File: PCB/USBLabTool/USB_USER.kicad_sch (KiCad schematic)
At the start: 15 parts, among them J19 USB_C_Receptacle, U17 TCPP01-M12

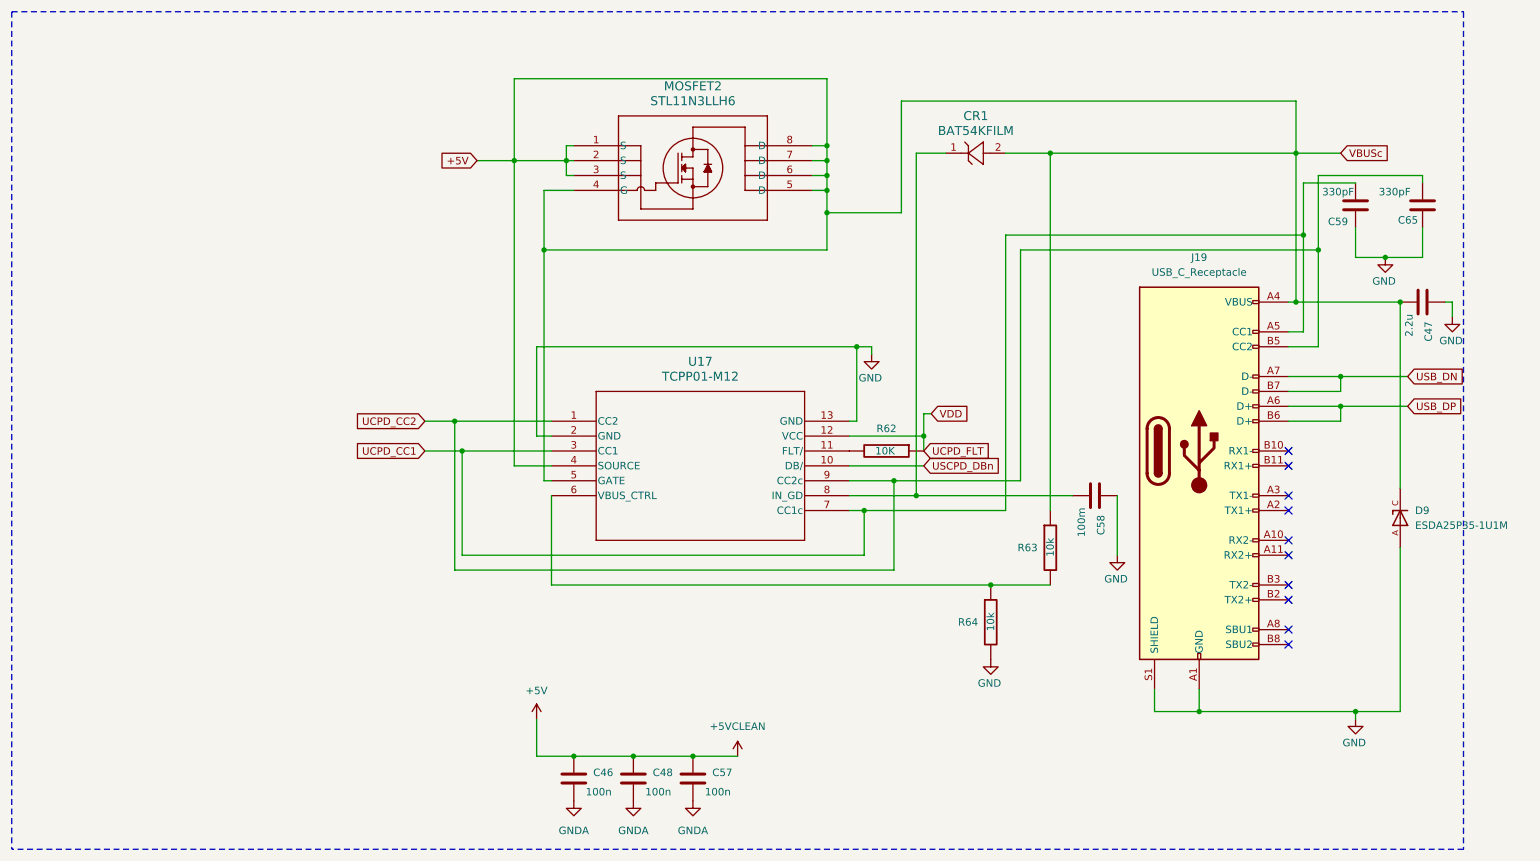
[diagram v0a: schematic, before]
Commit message: update MCU and USB, fix some footprints
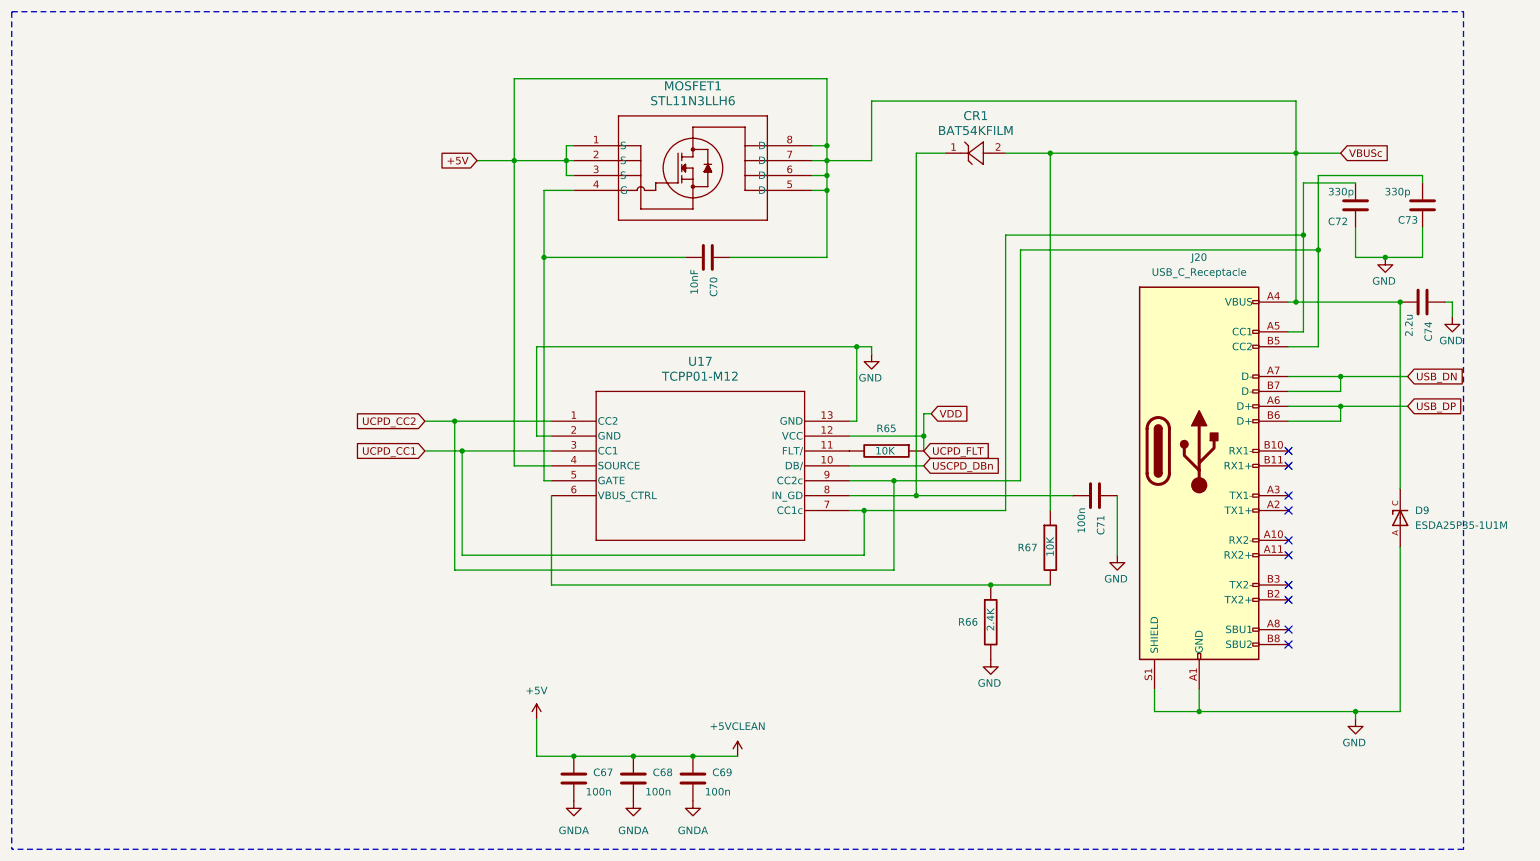
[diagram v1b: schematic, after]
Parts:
- added C70: 10nF, Capacitor_SMD:C_0603_1608Metric_Pad1.08x0.95mm_HandSolder, symbol Device:C
- C71: renamed from C58; value 100m -> 100n
- C72: renamed from C59; value 330pF -> 330p; footprint Capacitor_SMD:C_0603_1608Metric_Pad1.08x0.95mm_HandSolder -> Capacitor_SMD:C_0201_0603Metric_Pad0.64x0.40mm_HandSolder
- C73: renamed from C65; value 330pF -> 330p; footprint Capacitor_SMD:C_0603_1608Metric_Pad1.08x0.95mm_HandSolder -> Capacitor_SMD:C_0201_0603Metric_Pad0.64x0.40mm_HandSolder
- CR1: footprint SOD-523_STM -> Diode_SMD:D_SOD-523
- D9: footprint ESDA25P35-1U1M:TVS_ESDA25P35-1U1M -> footprintsgit:TVS_ESDA25P35-1U1M
- J20: renamed from J19; footprint footprints:CONN RCP USB3.1 TYPEC 24P SMD RA-632723300011 -> footprintsgit:CONN RCP USB3.1 TYPEC 24P SMD RA-632723300011
- R65: renamed from R62; footprint (none) -> Resistor_SMD:R_0603_1608Metric
- R66: renamed from R64; value 10k -> 2.4K; footprint (none) -> Resistor_SMD:R_0603_1608Metric
- R67: renamed from R63; value 10k -> 10K; footprint (none) -> Resistor_SMD:R_0603_1608Metric
- renumbered C46 to C67, C48 to C68, C57 to C69, C47 to C74, MOSFET2 to MOSFET1
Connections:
- net +5V: now also C70.1; no longer MOSFET1.4 (G), U17.5 (GATE)
- new net: C70.2, MOSFET1.4 (G), U17.5 (GATE)

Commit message: add usb protection
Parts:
- added D10: USBLC6-2SC6, PCM_Package_TO_SOT_SMD_AKL:SOT-23-6, symbol PCM_Diode_TVS_AKL:USBLC6-2SC6
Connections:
- net GND: now also D10.2 (VN)
- net USB_DN renamed D-
- net D-: now also D10.1 (L1), D10.6 (L1)
- net USB_DP renamed D+
- net D+: now also D10.3 (L2), D10.4 (L2)
- no-connect marks 10 -> 11
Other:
- moved on the sheet: R66

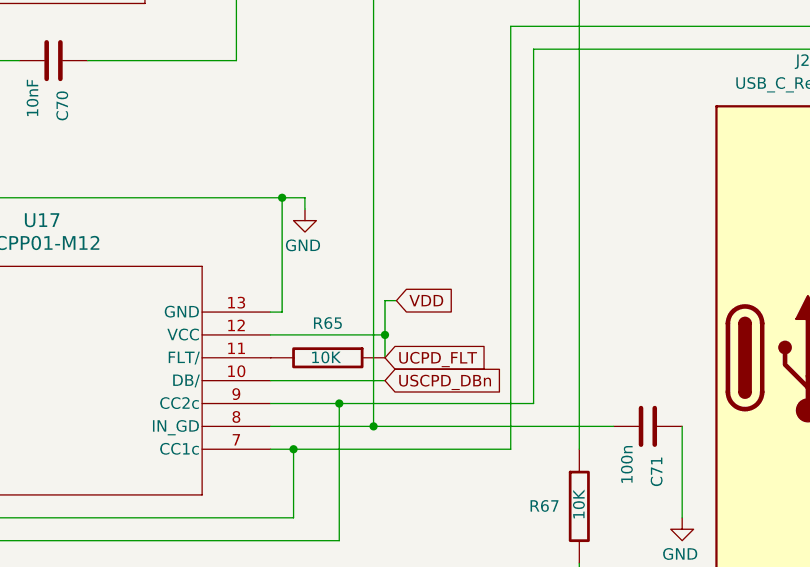
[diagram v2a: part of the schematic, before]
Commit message: add NRST button and change MCU pins as latest
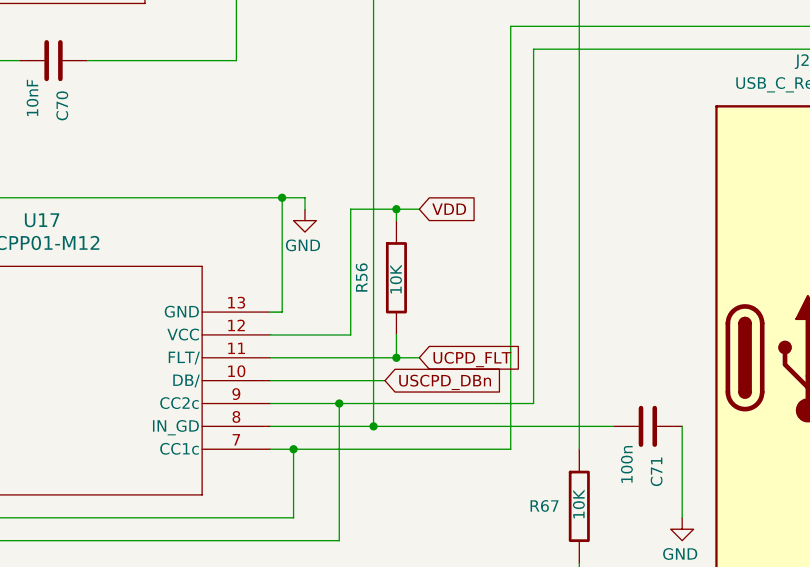
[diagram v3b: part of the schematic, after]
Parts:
- removed R65: 10K, Resistor_SMD:R_0603_1608Metric, symbol freetronics_schematic:R
- added R56: 10K, Resistor_SMD:R_0603_1608Metric, symbol freetronics_schematic:R
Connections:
- net UCPD_FLT: now also U17.11 (FLT/), R56.2; no longer U17.12 (VCC)
- new net VDD: R56.1, U17.12 (VCC)
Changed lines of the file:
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@@
 	)
 	(junction
+		(at 189.23 78.74)
+		(diameter 0)
+		(color 0 0 0 0)
+	)
+	(junction
 		(at 171.45 50.8)
 		(diameter 0)
@@
 	)
 	(junction
-		(at 251.46 44.45)
+		(at 189.23 95.25)
 		(diameter 0)
 		(color 0 0 0 0)
 	)
 	(junction
-		(at 171.45 48.26)
+		(at 251.46 44.45)
 		(diameter 0)
 		(color 0 0 0 0)
 	)
 	(junction
-		(at 176.53 77.47)
+		(at 171.45 48.26)
 		(diameter 0)
 		(color 0 0 0 0)
 	)
 	(junction
-		(at 187.96 92.71)
+		(at 176.53 77.47)
 		(diameter 0)
 		(color 0 0 0 0)
@@
 	(wire
 		(pts
-			(xy 187.96 88.9) (xy 187.96 92.71)
-		)
-		(stroke
-			(width 0)
-			(type default)
-		)
-	)
-	(wire
-		(pts
 			(xy 111.76 102.87) (xy 124.46 102.87)
 		)
@@
 	(wire
 		(pts
-			(xy 251.46 69.85) (xy 251.46 44.45)
+			(xy 184.15 78.74) (xy 184.15 92.71)
 		)
 		(stroke
@@
 	(wire
 		(pts
-			(xy 259.08 85.09) (xy 259.08 82.55)
+			(xy 251.46 69.85) (xy 251.46 44.45)
 		)
 		(stroke
@@
 	(wire
 		(pts
-			(xy 168.91 48.26) (xy 171.45 48.26)
+			(xy 259.08 85.09) (xy 259.08 82.55)
 		)
 		(stroke
@@
 	(wire
 		(pts
-			(xy 171.45 45.72) (xy 179.07 45.72)
+			(xy 168.91 48.26) (xy 171.45 48.26)
 		)
 		(stroke
@@
 	(wire
 		(pts
-			(xy 107.95 90.17) (xy 124.46 90.17)
+			(xy 171.45 45.72) (xy 179.07 45.72)
 		)
 		(stroke
@@
 	(wire
 		(pts
-			(xy 187.96 88.9) (xy 189.23 88.9)
+			(xy 107.95 90.17) (xy 124.46 90.17)
 		)
 		(stroke
@@
 	(wire
 		(pts
+			(xy 189.23 95.25) (xy 191.77 95.25)
+		)
+		(stroke
+			(width 0)
+			(type default)
+		)
+	)
+	(wire
+		(pts
 			(xy 255.27 60.96) (xy 255.27 48.26)
 		)
@@
 	(wire
 		(pts
+			(xy 184.15 78.74) (xy 189.23 78.74)
+		)
+		(stroke
+			(width 0)
+			(type default)
+		)
+	)
+	(wire
+		(pts
 			(xy 123.19 62.23) (xy 123.19 100.33)
 		)
@@
 	(wire
 		(pts
-			(xy 102.87 95.25) (xy 109.22 95.25)
+			(xy 189.23 78.74) (xy 189.23 80.01)
 		)
 		(stroke
@@
 	(wire
 		(pts
-			(xy 111.76 102.87) (xy 111.76 119.38)
+			(xy 102.87 95.25) (xy 109.22 95.25)
 		)
 		(stroke
@@
 	(wire
 		(pts
-			(xy 207.01 144.78) (xy 207.01 129.54)
+			(xy 111.76 102.87) (xy 111.76 119.38)
 		)
 		(stroke
@@
 	(wire
 		(pts
-			(xy 123.19 50.8) (xy 128.27 50.8)
+			(xy 207.01 144.78) (xy 207.01 129.54)
 		)
 		(stroke
@@
 	(wire
 		(pts
-			(xy 234.95 135.89) (xy 234.95 139.7)
+			(xy 123.19 50.8) (xy 128.27 50.8)
 		)
 		(stroke
@@
 	(wire
 		(pts
-			(xy 187.96 92.71) (xy 187.96 95.25)
+			(xy 234.95 135.89) (xy 234.95 139.7)
 		)
 		(stroke
@@
 	(wire
 		(pts
+			(xy 189.23 95.25) (xy 189.23 92.71)
+		)
+		(stroke
+			(width 0)
+			(type default)
+		)
+	)
+	(wire
+		(pts
 			(xy 182.88 129.54) (xy 185.42 129.54)
 		)
@@
 		)
 	)
+	(wire
+		(pts
+			(xy 189.23 78.74) (xy 191.77 78.74)
+		)
+		(stroke
+			(width 0)
+			(type default)
+		)
+	)
 	(polyline
 		(pts
@@
 	(wire
 		(pts
-			(xy 175.26 92.71) (xy 187.96 92.71)
-		)
-		(stroke
-			(width 0)
-			(type default)
-		)
-	)
-	(wire
-		(pts
 			(xy 118.11 45.72) (xy 118.11 97.79)
 		)
@@
 	(wire
 		(pts
+			(xy 175.26 95.25) (xy 189.23 95.25)
+		)
+		(stroke
+			(width 0)
+			(type default)
+		)
+	)
+	(wire
+		(pts
 			(xy 207.01 129.54) (xy 209.55 129.54)
 		)
@@
 	(wire
 		(pts
+			(xy 175.26 92.71) (xy 184.15 92.71)
+		)
+		(stroke
+			(width 0)
+			(type default)
+		)
+	)
+	(wire
+		(pts
 			(xy 128.27 147.32) (xy 138.43 147.32)
 		)
@@
 	(global_label "UCPD_FLT"
 		(shape input)
-		(at 187.96 95.25 0)
+		(at 191.77 95.25 0)
 		(fields_autoplaced yes)
 		(effects
@@
 		)
 		(property "Intersheetrefs" "${INTERSHEET_REFS}"
-			(at 200.1376 95.25 0)
+			(at 203.9476 95.25 0)
 			(effects
 				(font
@@
 	(global_label "VDD"
 		(shape input)
-		(at 189.23 88.9 0)
+		(at 191.77 78.74 0)
 		(fields_autoplaced yes)
 		(effects
@@
 		)
 		(property "Intersheetrefs" "${INTERSHEET_REFS}"
-			(at 195.8438 88.9 0)
+			(at 198.3838 78.74 0)
 			(effects
 				(font
@@
 	)
 	(symbol
+		(lib_id "freetronics_schematic:R")
+		(at 189.23 86.36 0)
+		(unit 1)
+		(exclude_from_sim no)
+		(in_bom yes)
+		(on_board yes)
+		(dnp no)
+		(property "Reference" "R56"
+			(at 185.42 86.36 90)
+			(effects
+				(font
+					(size 1.27 1.27)
+				)
+			)
+		)
+		(property "Value" "10K"
+			(at 189.23 86.614 90)
+			(effects
+				(font
+					(size 1.27 1.27)
+				)
+			)
+		)
+		(property "Footprint" "Resistor_SMD:R_0603_1608Metric"
+			(at 189.23 86.36 0)
+			(effects
+				(font
+					(size 1.524 1.524)
+				)
+				(hide yes)
+			)
+		)
+		(property "Datasheet" ""
+			(at 189.23 86.36 0)
+			(effects
+				(font
+					(size 1.524 1.524)
+				)
+				(hide yes)
+			)
+		)
+		(property "Description" "Resistor"
+			(at 189.23 86.36 0)
+			(effects
+				(font
+					(size 1.27 1.27)
+				)
+				(hide yes)
+			)
+		)
+		(property "Purpose" ""
+			(at 189.23 86.36 0)
+			(effects
+				(font
+					(size 1.27 1.27)
+				)
+				(hide yes)
+			)
+		)
+		(pin "1"
+		)
+		(pin "2"
+		)
+		(instances
+			(project "USBLabTool"
+				(path "/b5440f7d-90d5-417e-adc2-aa6b11e5424d/37e12e55-0596-42de-ac66-6f566cb1a838"
+					(reference "R56")
+					(unit 1)
+				)
+			)
+		)
+	)
+	(symbol
 		(lib_id "Device:C")
 		(at 261.62 53.34 180)
@@
 					(unit 1)
 				)
-			)
-		)
-	)
-	(symbol
-		(lib_id "freetronics_schematic:R")
-		(at 181.61 95.25 270)
-		(unit 1)
-		(exclude_from_sim no)
-		(in_bom yes)
-		(on_board yes)
-		(dnp no)
-		(property "Reference" "R65"
-			(at 181.61 91.44 90)
-			(effects
-				(font
-					(size 1.27 1.27)
-				)
-			)
-		)
-		(property "Value" "10K"
-			(at 181.356 95.25 90)
-			(effects
-				(font
-					(size 1.27 1.27)
-				)
-			)
-		)
-		(property "Footprint" "Resistor_SMD:R_0603_1608Metric"
-			(at 181.61 95.25 0)
-			(effects
-				(font
-					(size 1.524 1.524)
-				)
-				(hide yes)
-			)
-		)
-		(property "Datasheet" ""
-			(at 181.61 95.25 0)
-			(effects
-				(font
-					(size 1.524 1.524)
-				)
-				(hide yes)
-			)
-		)
-		(property "Description" "Resistor"
-			(at 181.61 95.25 0)
-			(effects
-				(font
-					(size 1.27 1.27)
-				)
-				(hide yes)
-			)
-		)
-		(property "Purpose" ""
-			(at 181.61 95.25 0)
-			(effects
-				(font
-					(size 1.27 1.27)
-				)
-				(hide yes)
-			)
-		)
-		(pin "1"
-		)
-		(pin "2"
-		)
-		(instances
-			(project ""
-				(path "/b5440f7d-90d5-417e-adc2-aa6b11e5424d/37e12e55-0596-42de-ac66-6f566cb1a838"
-					(reference "R65")
-					(unit 1)
-				)

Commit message: Fixed up footprints
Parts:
- D10: footprint PCM_Package_TO_SOT_SMD_AKL:SOT-23-6 -> userfp:SOT95P280X145-6N
- D9: footprint footprintsgit:TVS_ESDA25P35-1U1M -> userfp:TVS_ESDA25P35-1U1M
- J20: footprint footprintsgit:CONN RCP USB3.1 TYPEC 24P SMD RA-632723300011 -> userfp:CONN RCP USB3.1 TYPEC 24P SMD RA-632723300011
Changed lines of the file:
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@@
 			)
 		)
-		(property "Footprint" "PCM_Package_TO_SOT_SMD_AKL:SOT-23-6"
+		(property "Footprint" "userfp:SOT95P280X145-6N"
 			(at 195.58 144.78 0)
 			(effects
@@
 			)
 		)
-		(property "Footprint" "footprintsgit:CONN RCP USB3.1 TYPEC 24P SMD RA-632723300011"
+		(property "Footprint" "userfp:CONN RCP USB3.1 TYPEC 24P SMD RA-632723300011"
 			(at 238.76 95.25 0)
 			(effects
@@
 			)
 		)
-		(property "Footprint" "footprintsgit:TVS_ESDA25P35-1U1M"
+		(property "Footprint" "userfp:TVS_ESDA25P35-1U1M"
 			(at 269.24 106.68 0)
 			(effects

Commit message: minor fixes
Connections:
- net VDD renamed +3.3V

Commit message: footprint with minor fixes
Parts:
- J20: footprint userfp:CONN RCP USB3.1 TYPEC 24P SMD RA-632723300011 -> Connector_USB:USB_C_Receptacle_Amphenol_12401548E4-2A
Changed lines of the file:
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@@
 			)
 		)
-		(property "Footprint" "userfp:CONN RCP USB3.1 TYPEC 24P SMD RA-632723300011"
+		(property "Footprint" "Connector_USB:USB_C_Receptacle_Amphenol_12401548E4-2A"
 			(at 238.76 95.25 0)
 			(effects

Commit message: continue PCB layout
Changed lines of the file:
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@@
 (kicad_sch
-	(version 20231120)
+	(version 20250114)
 	(generator "eeschema")
-	(generator_version "8.0")
+	(generator_version "9.0")
 	(paper "A4")
 	(junction

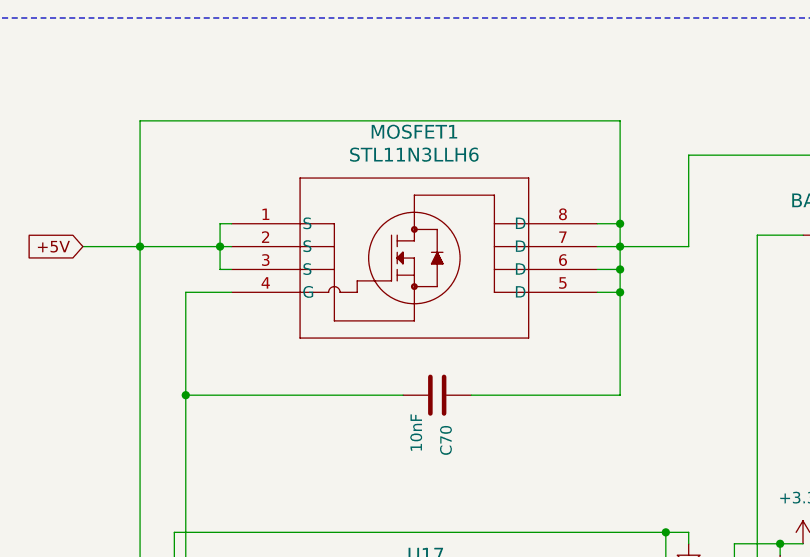
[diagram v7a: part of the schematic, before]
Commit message: change mosfet footprint
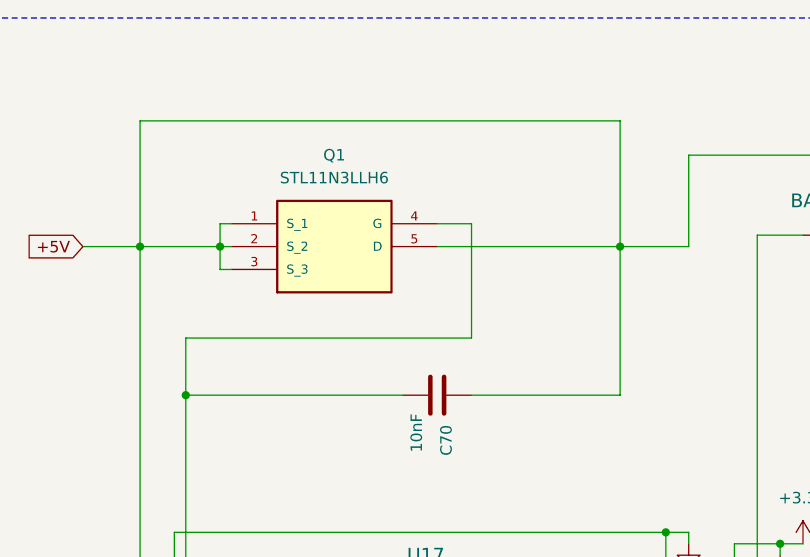
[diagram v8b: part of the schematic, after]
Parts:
- removed MOSFET1: STL11N3LLH6, POWERFLAT-3p3X3p3_STM, symbol STL11N3LLH6:STL11N3LLH6
- added Q1: STL11N3LLH6, userfp:STL20N6F7_snapmagic, symbol STL11N3LLH6_snapmagic:STL11N3LLH6
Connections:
- net +5V: now also Q1.1 (S_1), Q1.2 (S_2), Q1.3 (S_3), Q1.5 (D)
- net at C70.2, U17.5 (GATE): now also Q1.4 (G)
